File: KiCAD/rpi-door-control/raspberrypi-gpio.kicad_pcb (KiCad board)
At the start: 2 copper layers, 85 x 56 mm, 21 parts, among them J1 RJ45, P1 CONN_13X2, P2 CONN_2, P3 CONN_2, P4 CONN_2, Q1 N3904, SW1 SW_PUSH, U1 RELAY

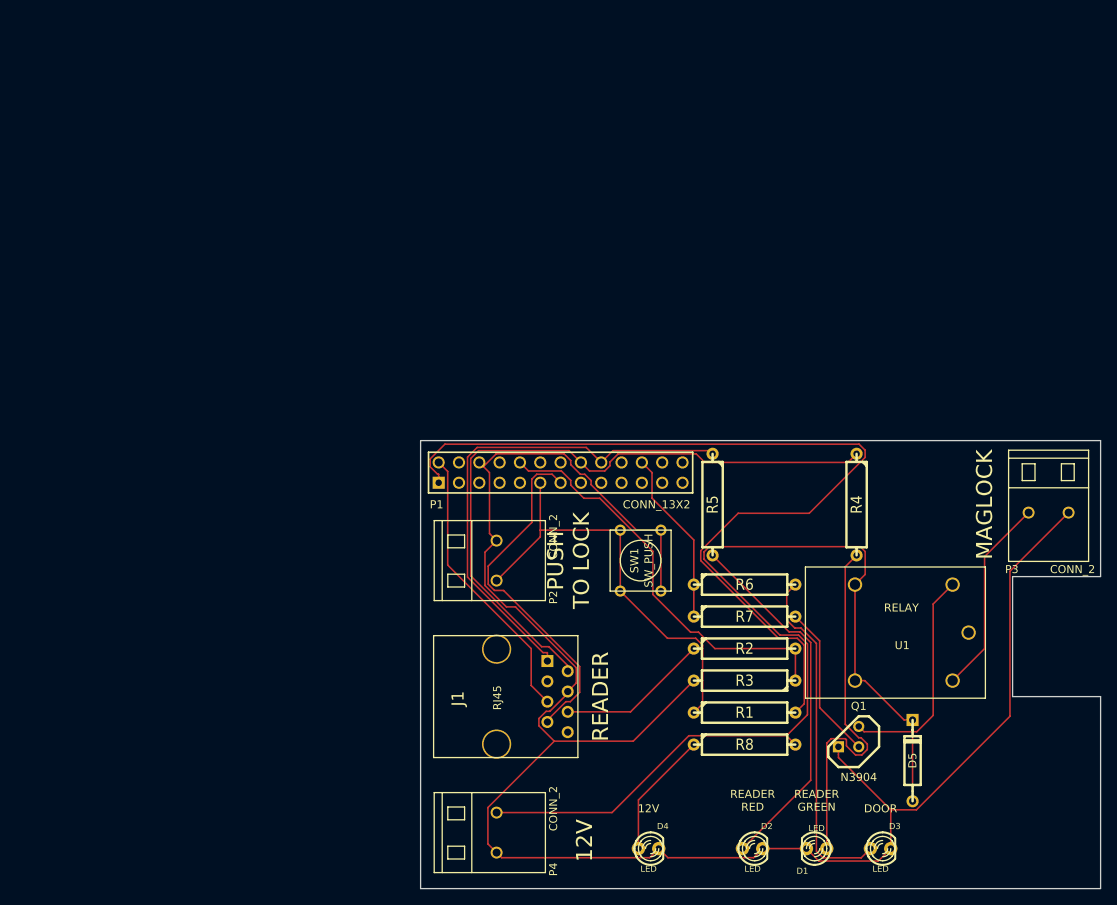
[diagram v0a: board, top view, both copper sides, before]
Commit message: Changed page size of pcb drawing
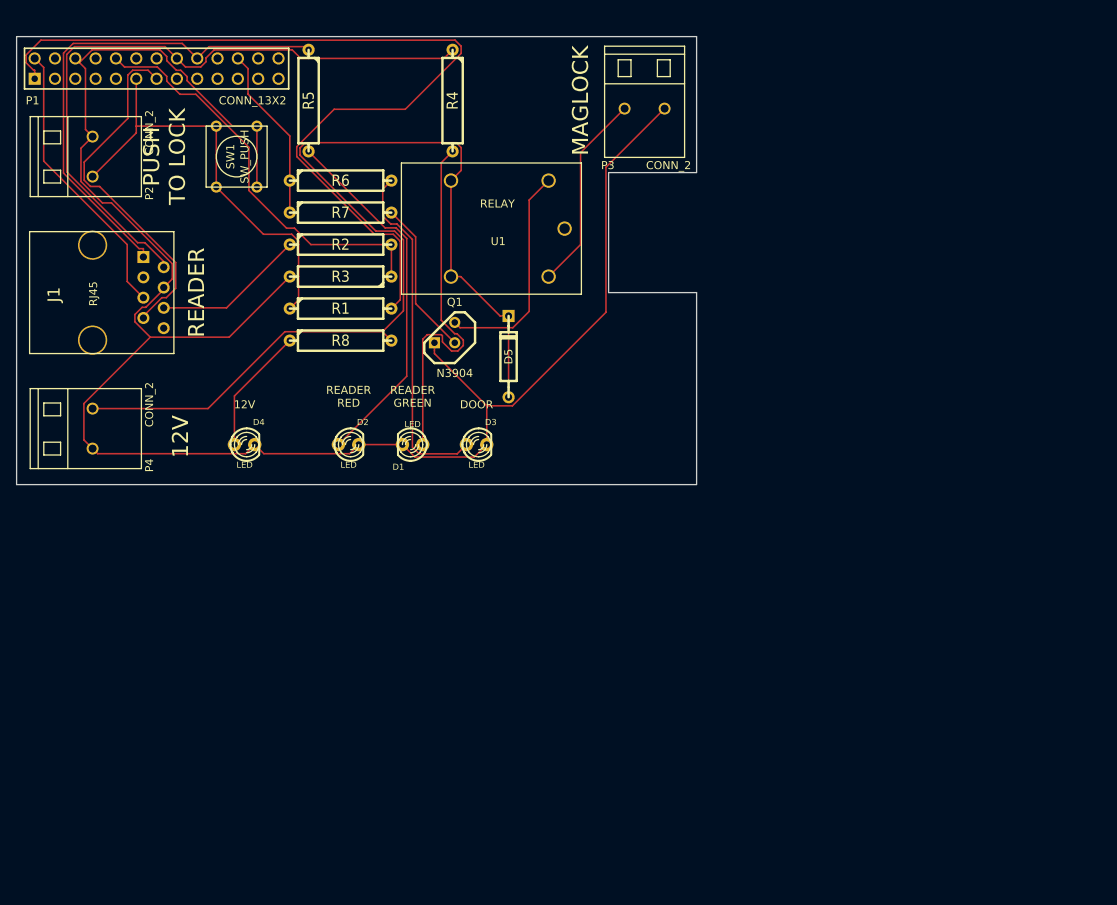
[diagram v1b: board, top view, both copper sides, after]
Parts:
- moved D1 71.4 mm to (142.5, 125.5)
- moved D2 71.4 mm to (134.5, 125.5)
- moved D3 71.4 mm to (150.5, 125.5)
- moved D4 71.4 mm to (121.5, 125.5)
- moved D5 71.4 mm to (154.5, 114.5)
- moved J1 71.4 mm to (102.5, 106.5)
- moved P1 71.4 mm to (110.5, 78.5)
- moved P2 71.4 mm to (102.5, 89.5)
- moved P3 71.4 mm to (171.5, 83.5)
- moved P4 71.4 mm to (102.5, 123.5)
- moved Q1 71.4 mm to (146.5, 111.5)
- moved R1 71.4 mm to (133.5, 108.5)
- moved R2 71.4 mm to (133.5, 100.5)
- moved R3 71.4 mm to (133.5, 104.5)
- moved R4 71.4 mm to (147.5, 82.5)
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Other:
- rule trace_min: 0.1524 -> 0.2

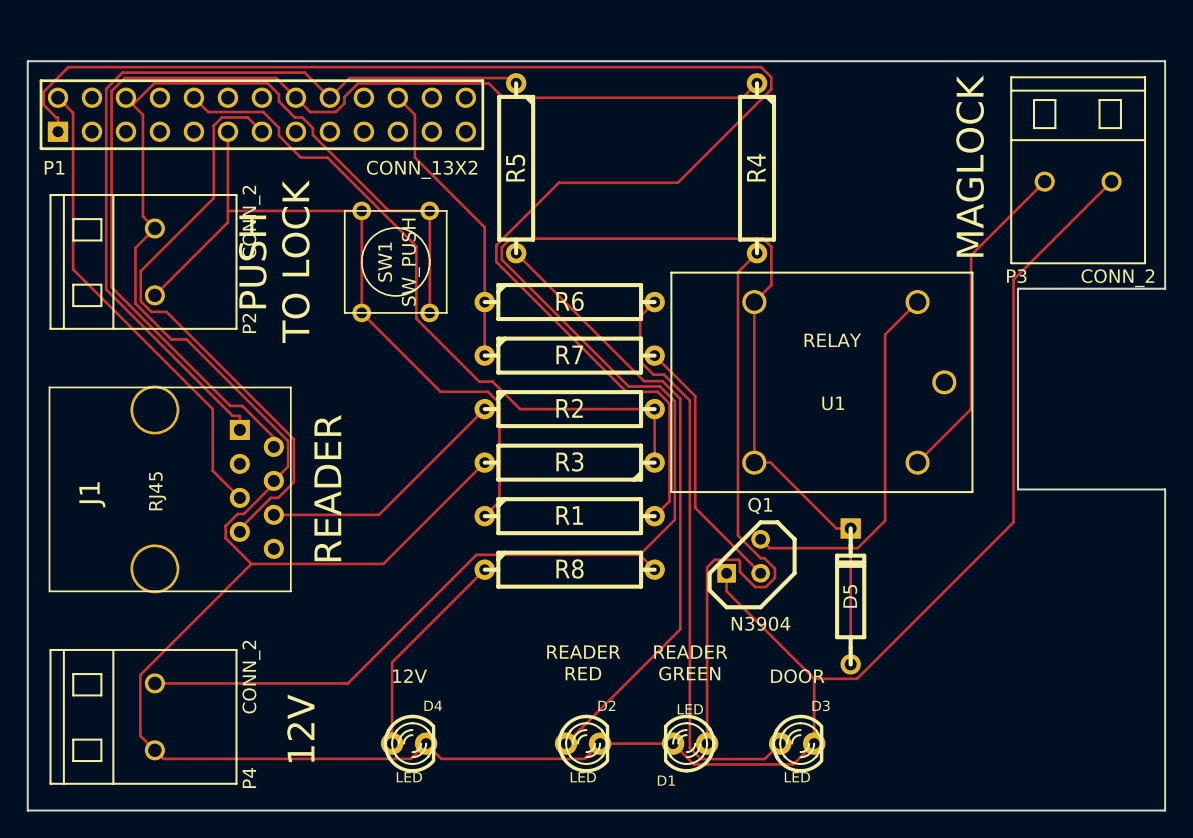
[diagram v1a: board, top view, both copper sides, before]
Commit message: Start of v0.5 of schematic.  Converted the circuit to isolate 12V with an opto-isolator.  Will redraw the PCB to be just a bullshit square linked by a ribbon cable or something so it can be milled with a 1.6mm cutter
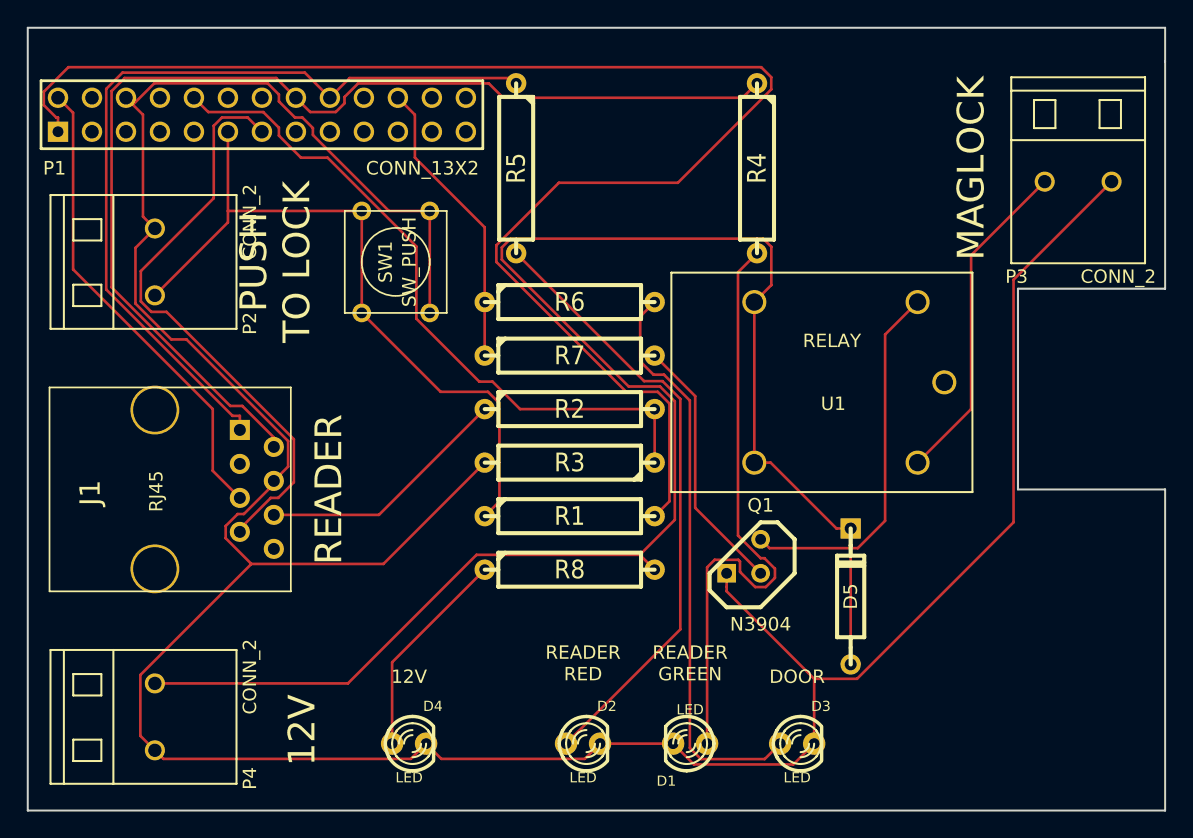
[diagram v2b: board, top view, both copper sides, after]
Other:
- board size 85 x 56 mm -> 85 x 58.5 mm
- net class Default: clearance 0.2 -> 0.5
- net class Power: clearance 0.2 -> 0.5
- rule trace_clearance: 0.2 -> 0.5
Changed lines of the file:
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@@
-(kicad_pcb (version 3) (host pcbnew "(2013-jul-07)-stable")
+(kicad_pcb (version 3) (host pcbnew "(2013-07-07 BZR 4022)-stable")
   (general
     (links 40)
     (no_connects 0)
-    (area 127.606667 112.000001 242.964763 190.8)
+    (area 78.541667 59.925001 192.464763 140.3)
     (thickness 1.6)
-    (drawings 50)
+    (drawings 51)
     (tracks 206)
     (zones 0)
@@
   (setup
     (last_trace_width 0.2)
-    (trace_clearance 0.2)
+    (trace_clearance 0.5)
     (zone_clearance 0.508)
     (zone_45_only no)
@@
   (net 18 N-000005)
   (net_class Default "This is the default net class."
-    (clearance 0.2)
+    (clearance 0.5)
     (trace_width 0.2)
     (via_dia 0.9)
@@
   )
   (net_class Power ""
-    (clearance 0.2)
+    (clearance 0.5)
     (trace_width 0.5)
     (via_dia 1)
@@
     )
   )
+  (gr_line (start 178 72) (end 178 74.5) (angle 90) (layer Edge.Cuts) (width 0.15))
+  (gr_line (start 93 72) (end 93 130.5) (angle 90) (layer Edge.Cuts) (width 0.15))
+  (gr_line (start 93 72) (end 178 72) (angle 90) (layer Edge.Cuts) (width 0.15))
+  (dimension 56 (width 0.25) (layer Dwgs.User)
+    (gr_text "56.000 mm" (at 83 102.5 90) (layer Dwgs.User)
+      (effects (font (size 1 1) (thickness 0.25)))
+    )
+    (feature1 (pts (xy 89.5 74.5) (xy 82 74.5)))
+    (feature2 (pts (xy 89.5 130.5) (xy 82 130.5)))
+    (crossbar (pts (xy 84 130.5) (xy 84 74.5)))
+    (arrow1a (pts (xy 84 74.5) (xy 84.58642 75.626503)))
+    (arrow1b (pts (xy 84 74.5) (xy 83.41358 75.626503)))
+    (arrow2a (pts (xy 84 130.5) (xy 84.58642 129.373497)))
+    (arrow2b (pts (xy 84 130.5) (xy 83.41358 129.373497)))
+  )
+  (dimension 85 (width 0.25) (layer Dwgs.User)
+    (gr_text "85.000 mm" (at 135.5 61.000001) (layer Dwgs.User)
+      (effects (font (size 1 1) (thickness 0.25)))
+    )
+    (feature1 (pts (xy 178 72) (xy 178 60.000001)))
+    (feature2 (pts (xy 93 72) (xy 93 60.000001)))
+    (crossbar (pts (xy 93 62.000001) (xy 178 62.000001)))
+    (arrow1a (pts (xy 178 62.000001) (xy 176.873497 62.586421)))
+    (arrow1b (pts (xy 178 62.000001) (xy 176.873497 61.413581)))
+    (arrow2a (pts (xy 93 62.000001) (xy 94.126503 62.586421)))
+    (arrow2b (pts (xy 93 62.000001) (xy 94.126503 61.413581)))
+  )
   (gr_text DOOR (at 150.5 120.5) (layer F.SilkS)
     (effects (font (size 1 1) (thickness 0.2)))
@@
   (gr_text "RASPBERRY-PI ADDON BOARD\nVIEW FROM TOP\nNOTE: P1 SHOULD BE FITTED ON THE REVERSE OF THE BOARD" (at 93.5 133) (layer Dwgs.User)
     (effects (font (size 2 1.7) (thickness 0.12)) (justify left))
-  )
-  (dimension 56 (width 0.12) (layer Dwgs.User)
-    (gr_text "56.000 mm" (at 132 153 90) (layer Dwgs.User)
-      (effects (font (size 1 1) (thickness 0.12)))
-    )
-    (feature1 (pts (xy 143.5 125) (xy 131 125)))
-    (feature2 (pts (xy 143.5 181) (xy 131 181)))
-    (crossbar (pts (xy 133 181) (xy 133 125)))
-    (arrow1a (pts (xy 133 125) (xy 133.58642 126.126503)))
-    (arrow1b (pts (xy 133 125) (xy 132.41358 126.126503)))
-    (arrow2a (pts (xy 133 181) (xy 133.58642 179.873497)))
-    (arrow2b (pts (xy 133 181) (xy 132.41358 179.873497)))
-  )
-  (dimension 85 (width 0.12) (layer Dwgs.User)
-    (gr_text "85.000 mm" (at 186 113.000001) (layer Dwgs.User)
-      (effects (font (size 1 1) (thickness 0.12)))
-    )
-    (feature1 (pts (xy 228.5 125) (xy 228.5 112.000001)))
-    (feature2 (pts (xy 143.5 125) (xy 143.5 112.000001)))
-    (crossbar (pts (xy 143.5 114.000001) (xy 228.5 114.000001)))
-    (arrow1a (pts (xy 228.5 114.000001) (xy 227.373497 114.586421)))
-    (arrow1b (pts (xy 228.5 114.000001) (xy 227.373497 113.413581)))
-    (arrow2a (pts (xy 143.5 114.000001) (xy 144.626503 114.586421)))
-    (arrow2b (pts (xy 143.5 114.000001) (xy 144.626503 113.413581)))
   )
   (gr_text "RCA\nREMOVE WITH\nSTD HEADERS\n!NO TH ABOVE!" (at 138 67.5) (layer Dwgs.User)
@@
   (gr_line (start 144 87.5) (end 144 74.5) (angle 90) (layer Dwgs.User) (width 0.2))
   (gr_line (start 132 74.5) (end 132 87.5) (angle 90) (layer Dwgs.User) (width 0.2))
-  (gr_line (start 178 74.5) (end 93 74.5) (angle 90) (layer Edge.Cuts) (width 0.15))
   (gr_line (start 93 130.5) (end 178 130.5) (angle 90) (layer Edge.Cuts) (width 0.15))
-  (gr_line (start 93 74.5) (end 93 130.5) (angle 90) (layer Edge.Cuts) (width 0.15))
   (segment (start 154.5 109.42) (end 153.4377 109.42) (width 0.2) (layer F.Cu) (net 1))
   (segment (start 148.5177 104.5) (end 147.3 104.5) (width 0.2) (layer F.Cu) (net 1))
